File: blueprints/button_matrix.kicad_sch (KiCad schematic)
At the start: 32 parts, among them SW1 SW_Push, SW10 SW_Push, SW11 SW_Push, SW12 SW_Push, SW13 SW_Push, SW14 SW_Push, SW15 SW_Push, SW16 SW_Push, SW2 SW_Push, SW3 SW_Push, SW4 SW_Push, SW5 SW_Push, SW6 SW_Push, SW7 SW_Push, SW8 SW_Push, SW9 SW_Push

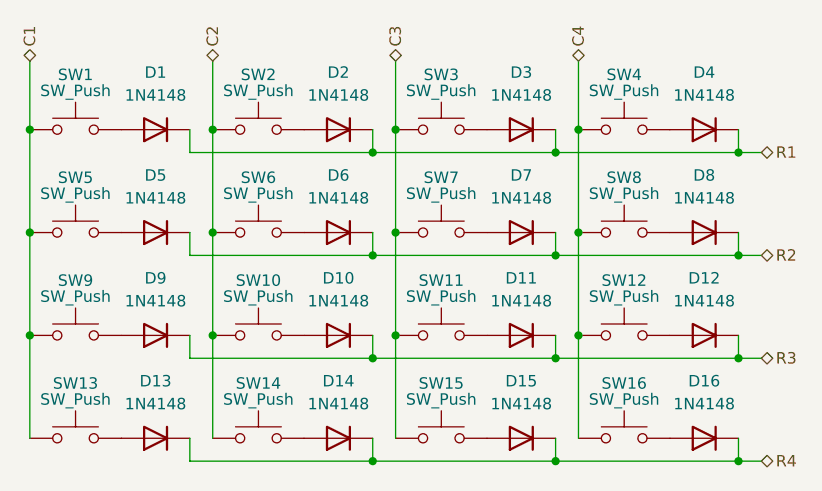
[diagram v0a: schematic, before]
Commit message: refactor: Change button matrix diodes form factor
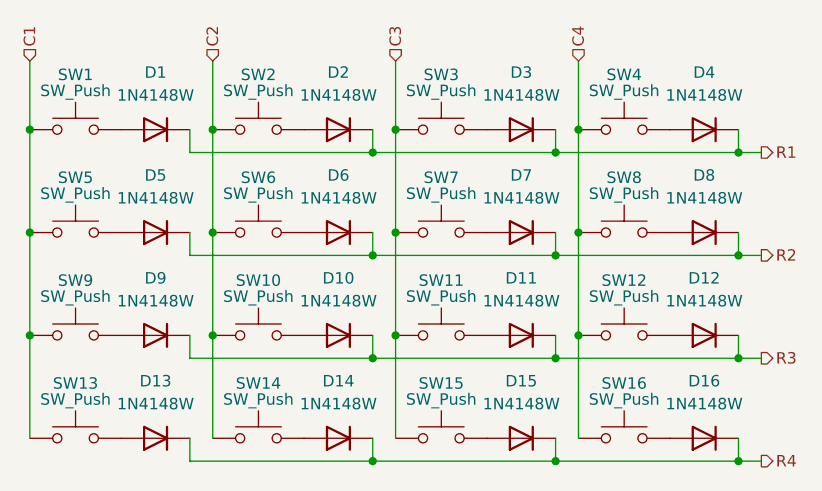
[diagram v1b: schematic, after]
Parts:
- removed D1, D10, D11, D12, D13, D14, D15, D16, D2, D3, D4, D5, D6, D7, D8, D9: 1N4148, Diode_THT:D_DO-35_SOD27_P7.62mm_Horizontal, symbol Diode:1N4148
- added D1, D10, D11, D12, D13, D14, D15, D16, D2, D3, D4, D5, D6, D7, D8, D9: 1N4148W, Diode_SMD:D_SOD-123, symbol Diode:1N4148W
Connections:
- net R1: now also D1.1 (K), D2.1 (K), D3.1 (K), D4.1 (K)
- net R2: now also D5.1 (K), D6.1 (K), D7.1 (K), D8.1 (K)
- net R3: now also D10.1 (K), D11.1 (K), D12.1 (K), D9.1 (K)
- net R4: now also D13.1 (K), D14.1 (K), D15.1 (K), D16.1 (K)
- net at SW9.2: now also D9.2 (A)
- net at SW7.2: now also D7.2 (A)
- net at SW10.2: now also D10.2 (A)
- net at SW16.2: now also D16.2 (A)
- net at SW3.2: now also D3.2 (A)
- net at SW4.2: now also D4.2 (A)
- net at SW2.2: now also D2.2 (A)
- net at SW8.2: now also D8.2 (A)
- net at SW15.2: now also D15.2 (A)
- net at SW11.2: now also D11.2 (A)
- net at SW13.2: now also D13.2 (A)
- net at SW12.2: now also D12.2 (A)
- net at SW1.2: now also D1.2 (A)
- net at SW14.2: now also D14.2 (A)
- net at SW5.2: now also D5.2 (A)
- net at SW6.2: now also D6.2 (A)
